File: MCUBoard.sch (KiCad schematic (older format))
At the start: 29 parts

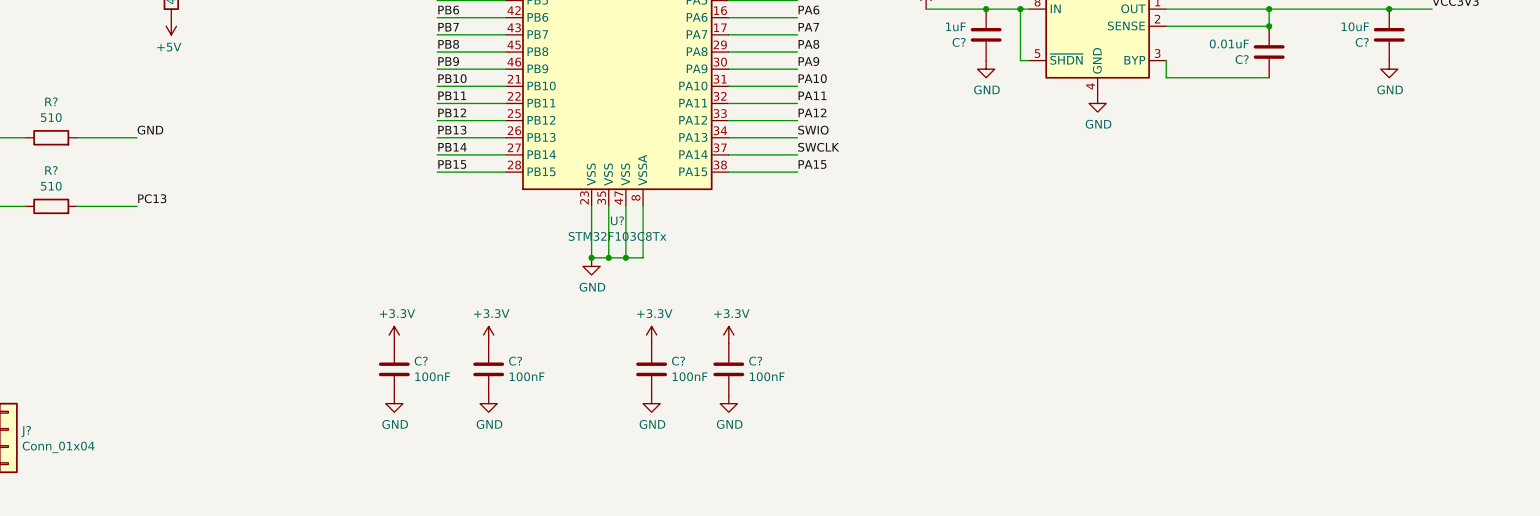
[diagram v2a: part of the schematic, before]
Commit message: added connector for 4D systems uLCD-144-G2
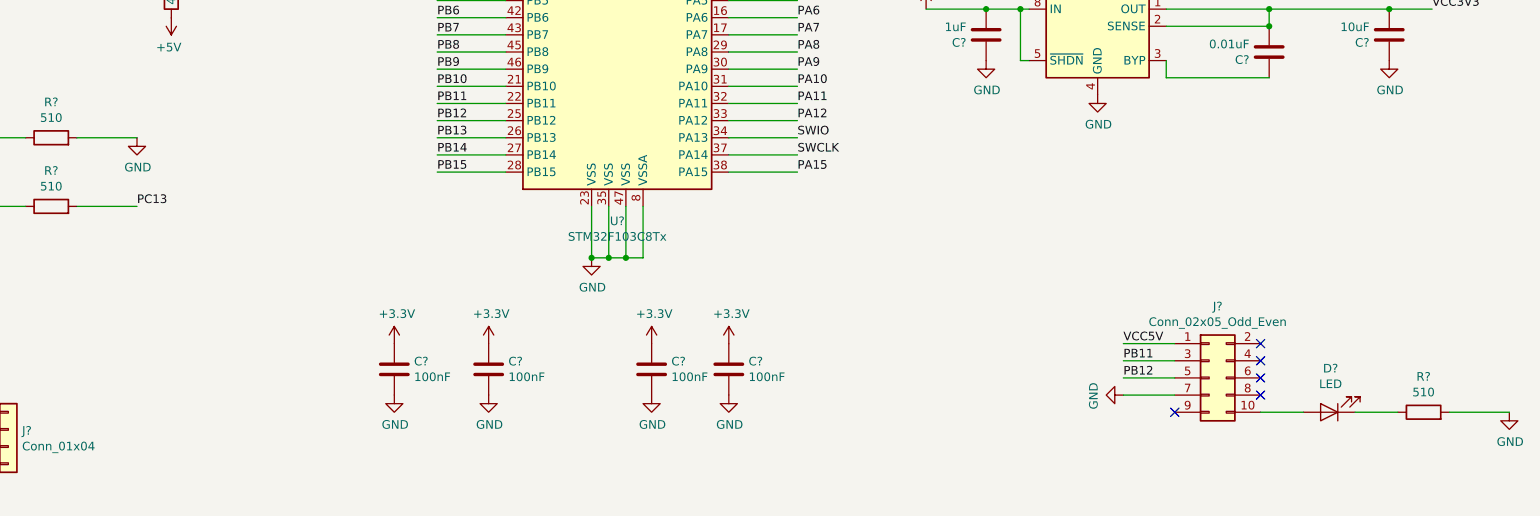
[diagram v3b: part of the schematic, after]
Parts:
- added D?: LED, symbol Device:LED
- added J?: Conn_02x05_Odd_Even, symbol Connector_Generic:Conn_02x05_Odd_Even
- added R?: 510, symbol Device:R
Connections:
- net +5V: now also J?.1 (Pin_1)
- net GND: now also J?.7 (Pin_7), R?.2
- net PB11: now also J?.3 (Pin_3)
- net PB12: now also J?.5 (Pin_5)
- new net: D?.2 (A), J?.10 (Pin_10)
- new net: D?.1 (K), R?.1
- no-connect marks 0 -> 5
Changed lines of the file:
@@
 $EndComp
 $Comp
-L power:GND #PWR?
+L power:GND #PWR0101
 U 1 1 5BB06098
 P 2050 2500
-F 0 "#PWR?" H 2050 2250 50  0001 C CNN
+F 0 "#PWR0101" H 2050 2250 50  0001 C CNN
 F 1 "GND" H 2055 2327 50  0000 C CNN
 F 2 "" H 2050 2500 50  0001 C CNN
@@
 $EndComp
 $Comp
-L power:GND #PWR?
+L power:GND #PWR0102
 U 1 1 5BB060B6
 P 2650 2500
-F 0 "#PWR?" H 2650 2250 50  0001 C CNN
+F 0 "#PWR0102" H 2650 2250 50  0001 C CNN
 F 1 "GND" H 2655 2327 50  0000 C CNN
 F 2 "" H 2650 2500 50  0001 C CNN
@@
 $EndComp
 $Comp
-L power:+3.3V #PWR?
+L power:+3.3V #PWR0103
 U 1 1 5BB06309
 P 2800 2000
-F 0 "#PWR?" H 2800 1850 50  0001 C CNN
+F 0 "#PWR0103" H 2800 1850 50  0001 C CNN
 F 1 "+3.3V" H 2815 2173 50  0000 C CNN
 F 2 "" H 2800 2000 50  0001 C CNN
@@
 BOOT1
 $Comp
-L power:+3.3V #PWR?
+L power:+3.3V #PWR0104
 U 1 1 5BB06604
 P 1900 2000
-F 0 "#PWR?" H 1900 1850 50  0001 C CNN
+F 0 "#PWR0104" H 1900 1850 50  0001 C CNN
 F 1 "+3.3V" H 1915 2173 50  0000 C CNN
 F 2 "" H 1900 2000 50  0001 C CNN
@@
 $EndComp
 $Comp
-L power:+5V #PWR?
+L power:+5V #PWR0105
 U 1 1 5BB0696A
 P 1800 2950
-F 0 "#PWR?" H 1800 2800 50  0001 C CNN
+F 0 "#PWR0105" H 1800 2800 50  0001 C CNN
 F 1 "+5V" H 1815 3123 50  0000 C CNN
 F 2 "" H 1800 2950 50  0001 C CNN
@@
 $EndComp
 $Comp
-L power:GND #PWR?
+L power:GND #PWR0106
 U 1 1 5BB07237
 P 1750 3500
-F 0 "#PWR?" H 1750 3250 50  0001 C CNN
+F 0 "#PWR0106" H 1750 3250 50  0001 C CNN
 F 1 "GND" H 1755 3327 50  0000 C CNN
 F 2 "" H 1750 3500 50  0001 C CNN
@@
 	2850 3500 2850 3400
 $Comp
-L power:+5V #PWR?
+L power:+5V #PWR0107
 U 1 1 5BB07FD5
 P 2850 3800
-F 0 "#PWR?" H 2850 3650 50  0001 C CNN
+F 0 "#PWR0107" H 2850 3650 50  0001 C CNN
 F 1 "+5V" H 2865 3973 50  0000 C CNN
 F 2 "" H 2850 3800 50  0001 C CNN
@@
 $EndComp
 $Comp
-L power:+3.3V #PWR?
+L power:+3.3V #PWR0108
 U 1 1 5BB08511
 P 1200 4400
-F 0 "#PWR?" H 1200 4250 50  0001 C CNN
+F 0 "#PWR0108" H 1200 4250 50  0001 C CNN
 F 1 "+3.3V" H 1215 4573 50  0000 C CNN
 F 2 "" H 1200 4400 50  0001 C CNN
@@
 $EndComp
 $Comp
-L power:+3.3V #PWR?
+L power:+3.3V #PWR0109
 U 1 1 5BB08530
 P 1200 4800
-F 0 "#PWR?" H 1200 4650 50  0001 C CNN
+F 0 "#PWR0109" H 1200 4650 50  0001 C CNN
 F 1 "+3.3V" H 1215 4973 50  0000 C CNN
 F 2 "" H 1200 4800 50  0001 C CNN
@@
 Wire Wire Line
 	2300 4900 2650 4900
-Text Label 2650 4500 0    50   ~ 0
-GND
 Text Label 2650 4900 0    50   ~ 0
 PC13
 $Comp
-L power:+3.3V #PWR?
+L power:+3.3V #PWR0110
 U 1 1 5BB09C56
 P 4150 5700
-F 0 "#PWR?" H 4150 5550 50  0001 C CNN
+F 0 "#PWR0110" H 4150 5550 50  0001 C CNN
 F 1 "+3.3V" H 4165 5873 50  0000 C CNN
 F 2 "" H 4150 5700 50  0001 C CNN
@@
 $EndComp
 $Comp
-L power:GND #PWR?
+L power:GND #PWR0111
 U 1 1 5BB09DA4
 P 4150 6000
-F 0 "#PWR?" H 4150 5750 50  0001 C CNN
+F 0 "#PWR0111" H 4150 5750 50  0001 C CNN
 F 1 "GND" H 4155 5827 50  0000 C CNN
 F 2 "" H 4150 6000 50  0001 C CNN
@@
 $EndComp
 $Comp
-L power:+3.3V #PWR?
+L power:+3.3V #PWR0112
 U 1 1 5BB0A29E
 P 4700 5700
-F 0 "#PWR?" H 4700 5550 50  0001 C CNN
+F 0 "#PWR0112" H 4700 5550 50  0001 C CNN
 F 1 "+3.3V" H 4715 5873 50  0000 C CNN
 F 2 "" H 4700 5700 50  0001 C CNN
@@
 $EndComp
 $Comp
-L power:GND #PWR?
+L power:GND #PWR0113
 U 1 1 5BB0A2AB
 P 4700 6000
-F 0 "#PWR?" H 4700 5750 50  0001 C CNN
+F 0 "#PWR0113" H 4700 5750 50  0001 C CNN
 F 1 "GND" H 4705 5827 50  0000 C CNN
 F 2 "" H 4700 6000 50  0001 C CNN
@@
 $EndComp
 $Comp
-L power:+3.3V #PWR?
+L power:+3.3V #PWR0114
 U 1 1 5BB0A73C
 P 5650 5700
-F 0 "#PWR?" H 5650 5550 50  0001 C CNN
+F 0 "#PWR0114" H 5650 5550 50  0001 C CNN
 F 1 "+3.3V" H 5665 5873 50  0000 C CNN
 F 2 "" H 5650 5700 50  0001 C CNN
@@
 $EndComp
 $Comp
-L power:GND #PWR?
+L power:GND #PWR0115
 U 1 1 5BB0A749
 P 5650 6000
-F 0 "#PWR?" H 5650 5750 50  0001 C CNN
+F 0 "#PWR0115" H 5650 5750 50  0001 C CNN
 F 1 "GND" H 5655 5827 50  0000 C CNN
 F 2 "" H 5650 6000 50  0001 C CNN
@@
 $EndComp
 $Comp
-L power:+3.3V #PWR?
+L power:+3.3V #PWR0116
 U 1 1 5BB0ABDA
 P 6100 5700
-F 0 "#PWR?" H 6100 5550 50  0001 C CNN
+F 0 "#PWR0116" H 6100 5550 50  0001 C CNN
 F 1 "+3.3V" H 6115 5873 50  0000 C CNN
 F 2 "" H 6100 5700 50  0001 C CNN
@@
 $EndComp
 $Comp
-L power:GND #PWR?
+L power:GND #PWR0117
 U 1 1 5BB0ABE7
 P 6100 6000
-F 0 "#PWR?" H 6100 5750 50  0001 C CNN
+F 0 "#PWR0117" H 6100 5750 50  0001 C CNN
 F 1 "GND" H 6105 5827 50  0000 C CNN
 F 2 "" H 6100 6000 50  0001 C CNN
@@
 PC14
 $Comp
-L power:GND #PWR?
+L power:GND #PWR0118
 U 1 1 5BB0CAB3
 P 7500 2400
-F 0 "#PWR?" H 7500 2150 50  0001 C CNN
+F 0 "#PWR0118" H 7500 2150 50  0001 C CNN
 F 1 "GND" H 7505 2227 50  0000 C CNN
 F 2 "" H 7500 2400 50  0001 C CNN
@@
 SWDCLK
 $Comp
-L power:+3.3V #PWR?
+L power:+3.3V #PWR0119
 U 1 1 5BB2C7FE
 P 1150 6100
-F 0 "#PWR?" H 1150 5950 50  0001 C CNN
+F 0 "#PWR0119" H 1150 5950 50  0001 C CNN
 F 1 "+3.3V" H 1165 6273 50  0000 C CNN
 F 2 "" H 1150 6100 50  0001 C CNN
@@
 	1150 6100 1700 6100
 $Comp
-L power:GND #PWR?
+L power:GND #PWR0120
 U 1 1 5BB2C83D
 P 1150 6400
-F 0 "#PWR?" H 1150 6150 50  0001 C CNN
+F 0 "#PWR0120" H 1150 6150 50  0001 C CNN
 F 1 "GND" H 1155 6227 50  0000 C CNN
 F 2 "" H 1150 6400 50  0001 C CNN
@@
 Connection ~ 9250 3750
 $Comp
-L power:GND #PWR?
+L power:GND #PWR0121
 U 1 1 5BB3BDE6
 P 8250 4250
-F 0 "#PWR?" H 8250 4000 50  0001 C CNN
+F 0 "#PWR0121" H 8250 4000 50  0001 C CNN
 F 1 "GND" H 8255 4077 50  0000 C CNN
 F 2 "" H 8250 4250 50  0001 C CNN
@@
 $EndComp
 $Comp
-L power:GND #PWR?
+L power:GND #PWR0122
 U 1 1 5BB3BE2B
 P 7600 4050
-F 0 "#PWR?" H 7600 3800 50  0001 C CNN
+F 0 "#PWR0122" H 7600 3800 50  0001 C CNN
 F 1 "GND" H 7605 3877 50  0000 C CNN
 F 2 "" H 7600 4050 50  0001 C CNN
@@
 $EndComp
 $Comp
-L power:GND #PWR?
+L power:GND #PWR0123
 U 1 1 5BB3BE70
 P 9950 4050
-F 0 "#PWR?" H 9950 3800 50  0001 C CNN
+F 0 "#PWR0123" H 9950 3800 50  0001 C CNN
 F 1 "GND" H 9955 3877 50  0000 C CNN
 F 2 "" H 9950 4050 50  0001 C CNN
@@
 $EndComp
 $Comp
-L power:+5V #PWR?
+L power:+5V #PWR0124
 U 1 1 5BB3C133
 P 7250 3750
-F 0 "#PWR?" H 7250 3600 50  0001 C CNN
+F 0 "#PWR0124" H 7250 3600 50  0001 C CNN
 F 1 "+5V" H 7265 3923 50  0000 C CNN
 F 2 "" H 7250 3750 50  0001 C CNN
@@
 VCC3V3
 $Comp
-L power:GND #PWR?
+L power:GND #PWR0125
 U 1 1 5BB4C12D
 P 5300 5200
-F 0 "#PWR?" H 5300 4950 50  0001 C CNN
+F 0 "#PWR0125" H 5300 4950 50  0001 C CNN
 F 1 "GND" H 5305 5027 50  0000 C CNN
 F 2 "" H 5300 5200 50  0001 C CNN
@@
 Wire Wire Line
 	5500 5200 5600 5200
+$Comp
+L Connector_Generic:Conn_02x05_Odd_Even J?
+U 1 1 5BB50FD8
+P 8900 5900
+F 0 "J?" H 8950 6317 50  0000 C CNN
+F 1 "Conn_02x05_Odd_Even" H 8950 6226 50  0000 C CNN
+F 2 "" H 8900 5900 50  0001 C CNN
+F 3 "~" H 8900 5900 50  0001 C CNN
+	1    8900 5900
+	1    0    0    -1
+$EndComp
+Wire Wire Line
+	8700 5700 8400 5700
+Wire Wire Line
+	8700 5800 8400 5800
+Wire Wire Line
+	8700 5900 8400 5900
+Wire Wire Line
+	8700 6000 8400 6000
+NoConn ~ 9200 5700
+Text Label 8400 5700 0    50   ~ 0
+VCC5V
+Text Label 8400 5800 0    50   ~ 0
+PB11
+Text Label 8400 5900 0    50   ~ 0
+PB12
+$Comp
+L power:GND #PWR?
+U 1 1 5BB91085
+P 8400 6000
+F 0 "#PWR?" H 8400 5750 50  0001 C CNN
+F 1 "GND" H 8405 5827 50  0000 C CNN
+F 2 "" H 8400 6000 50  0001 C CNN
+F 3 "" H 8400 6000 50  0001 C CNN
+	1    8400 6000
+	0    1    1    0
+$EndComp
+NoConn ~ 8700 6100
+NoConn ~ 9200 5800
+NoConn ~ 9200 5900
+NoConn ~ 9200 6000
+$Comp
+L Device:LED D?
+U 1 1 5BBA6862
+P 9600 6100
+F 0 "D?" H 9592 5845 50  0000 C CNN
+F 1 "LED" H 9592 5936 50  0000 C CNN
+F 2 "" H 9600 6100 50  0001 C CNN
+F 3 "~" H 9600 6100 50  0001 C CNN
+	1    9600 6100
+	-1   0    0    1
+$EndComp
+$Comp
+L Device:R R?
+U 1 1 5BBA686F
+P 10150 6100
+F 0 "R?" V 10357 6100 50  0000 C CNN
+F 1 "510" V 10266 6100 50  0000 C CNN
+F 2 "" V 10080 6100 50  0001 C CNN
+F 3 "~" H 10150 6100 50  0001 C CNN
+	1    10150 6100
+	0    -1   -1   0
+$EndComp
+Wire Wire Line
+	9200 6100 9450 6100
+Wire Wire Line
+	9750 6100 10000 6100
+Wire Wire Line
+	10300 6100 10650 6100
+$Comp
+L power:GND #PWR?
+U 1 1 5BBB15E1
+P 2650 4500
+F 0 "#PWR?" H 2650 4250 50  0001 C CNN
+F 1 "GND" H 2655 4327 50  0000 C CNN
+F 2 "" H 2650 4500 50  0001 C CNN
+F 3 "" H 2650 4500 50  0001 C CNN
+	1    2650 4500
+	1    0    0    -1
+$EndComp
+$Comp
+L power:GND #PWR?
+U 1 1 5BBB162C
+P 10650 6100
+F 0 "#PWR?" H 10650 5850 50  0001 C CNN
+F 1 "GND" H 10655 5927 50  0000 C CNN
+F 2 "" H 10650 6100 50  0001 C CNN
+F 3 "" H 10650 6100 50  0001 C CNN
+	1    10650 6100
+	1    0    0    -1
+$EndComp
 $EndSCHEMATC

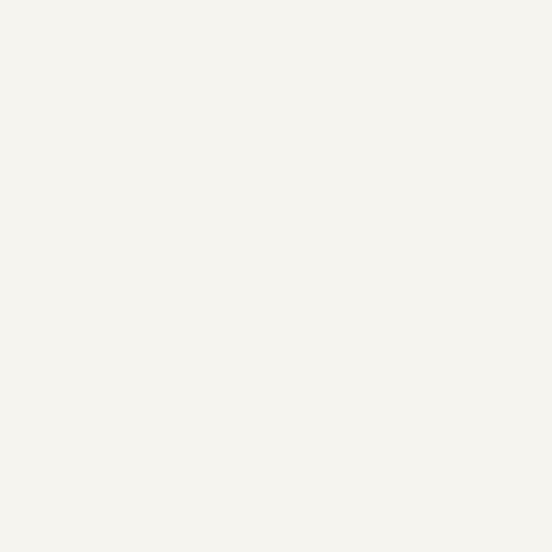
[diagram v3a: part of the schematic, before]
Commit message: 5V-3.3V bidirectional level shifter
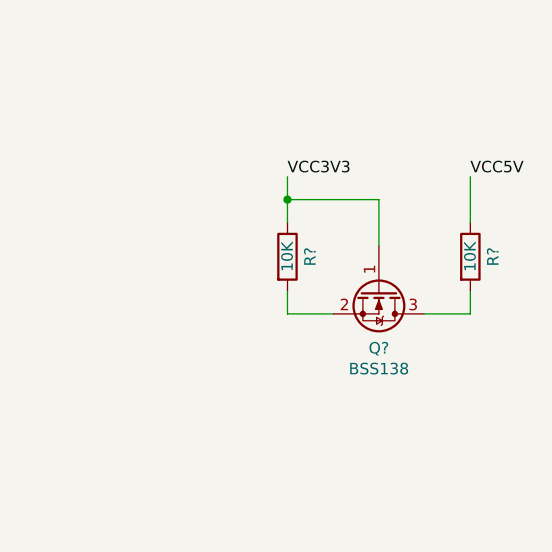
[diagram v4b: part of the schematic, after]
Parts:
- added Q?: BSS138, Package_TO_SOT_SMD:SOT-23, symbol Transistor_FET:BSS138
- added R? (x2): 10K, symbol Device:R
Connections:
- net +5V: now also R?.1
- net VCC3V3: now also Q?.1 (G), R?.1
- new net: Q?.2 (S), R?.2
- new net: Q?.3 (D), R?.2
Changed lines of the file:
@@
 	1    0    0    -1
 $EndComp
+$Comp
+L Device:R R?
+U 1 1 5BBC27EC
+P 11400 2150
+F 0 "R?" V 11500 2150 50  0000 C CNN
+F 1 "10K" V 11400 2150 50  0000 C CNN
+F 2 "" V 11330 2150 50  0001 C CNN
+F 3 "~" H 11400 2150 50  0001 C CNN
+	1    11400 2150
+	1    0    0    -1
+$EndComp
+$Comp
+L Transistor_FET:BSS138 Q?
+U 1 1 5BBC2A16
+P 11800 2300
+F 0 "Q?" V 12050 2300 50  0000 C CNN
+F 1 "BSS138" V 12141 2300 50  0000 C CNN
+F 2 "Package_TO_SOT_SMD:SOT-23" H 12000 2225 50  0001 L CIN
+F 3 "https://www.fairchildsemi.com/datasheets/BS/BSS138.pdf" H 11800 2300 50  0001 L CNN
+	1    11800 2300
+	0    1    1    0
+$EndComp
+$Comp
+L Device:R R?
+U 1 1 5BBCDFE2
+P 12200 2150
+F 0 "R?" V 12300 2150 50  0000 C CNN
+F 1 "10K" V 12200 2150 50  0000 C CNN
+F 2 "" V 12130 2150 50  0001 C CNN
+F 3 "~" H 12200 2150 50  0001 C CNN
+	1    12200 2150
+	1    0    0    -1
+$EndComp
+Wire Wire Line
+	11400 1800 11400 1900
+Wire Wire Line
+	11400 2300 11400 2400
+Wire Wire Line
+	11400 2400 11600 2400
+Wire Wire Line
+	12000 2400 12200 2400
+Wire Wire Line
+	12200 2400 12200 2300
+Wire Wire Line
+	11400 1900 11800 1900
+Wire Wire Line
+	11800 1900 11800 2100
+Connection ~ 11400 1900
+Wire Wire Line
+	11400 1900 11400 2000
+Wire Wire Line
+	12200 2000 12200 1800
+Text Label 11400 1800 0    50   ~ 0
+VCC3V3
+Text Label 12200 1800 0    50   ~ 0
+VCC5V
 $EndSCHEMATC

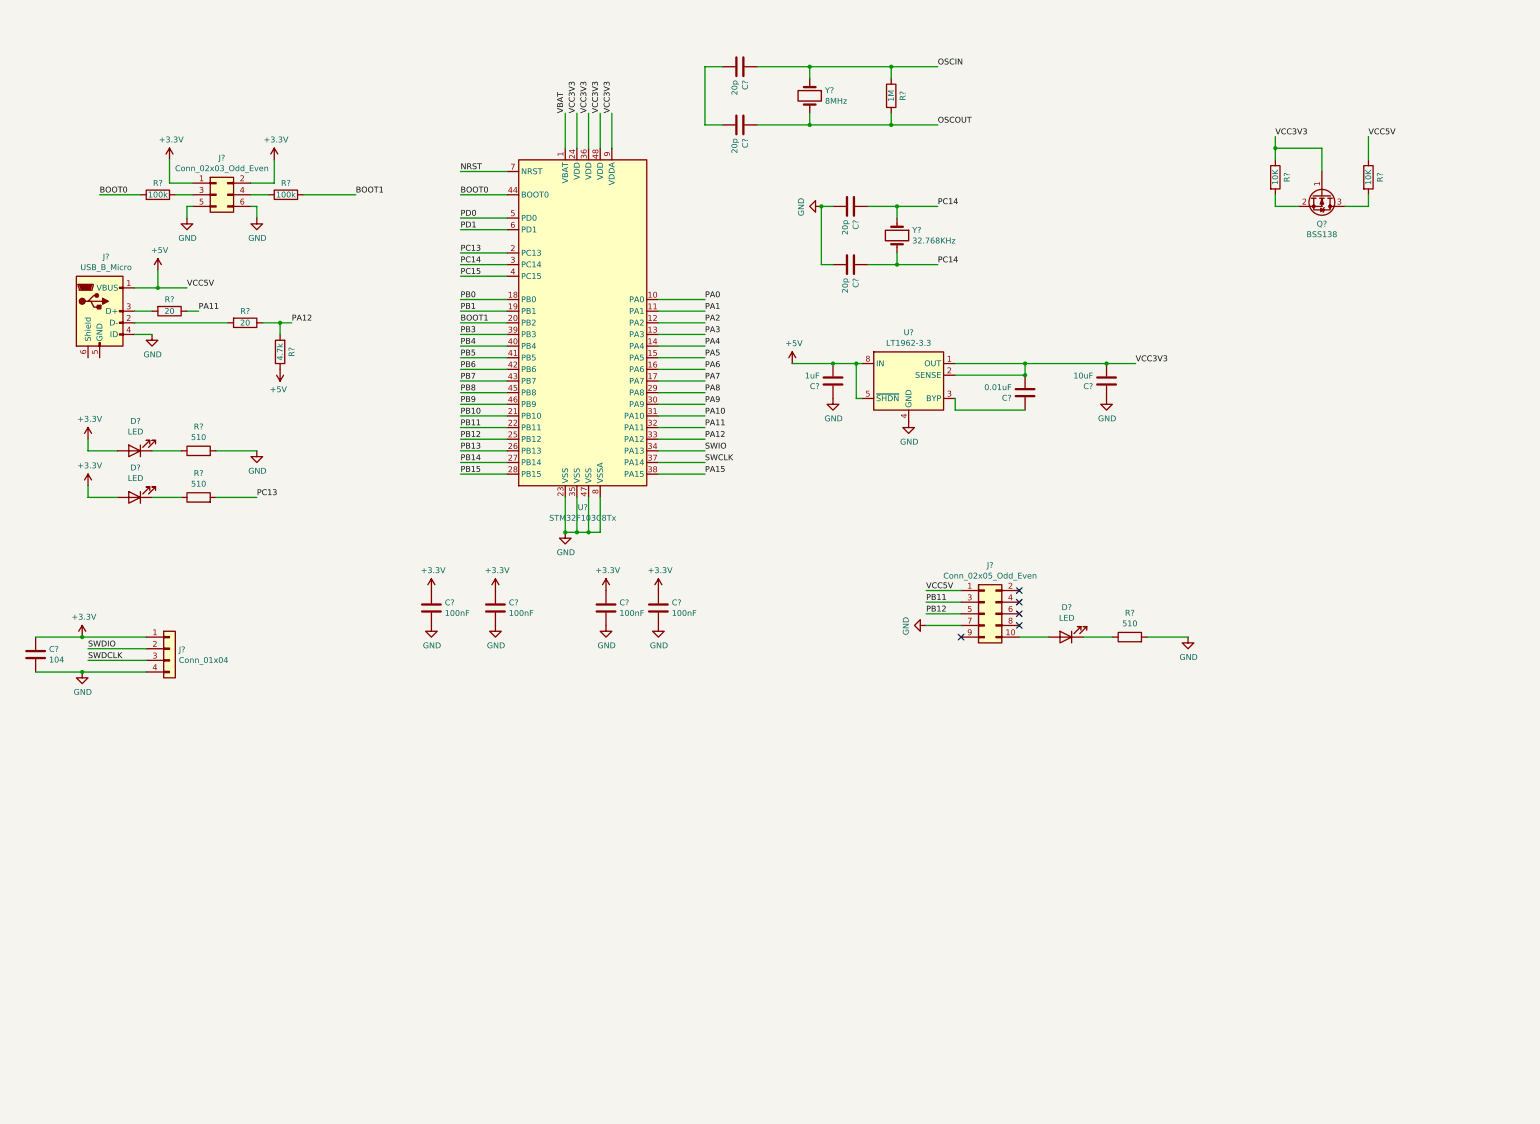
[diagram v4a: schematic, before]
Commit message: add opamps
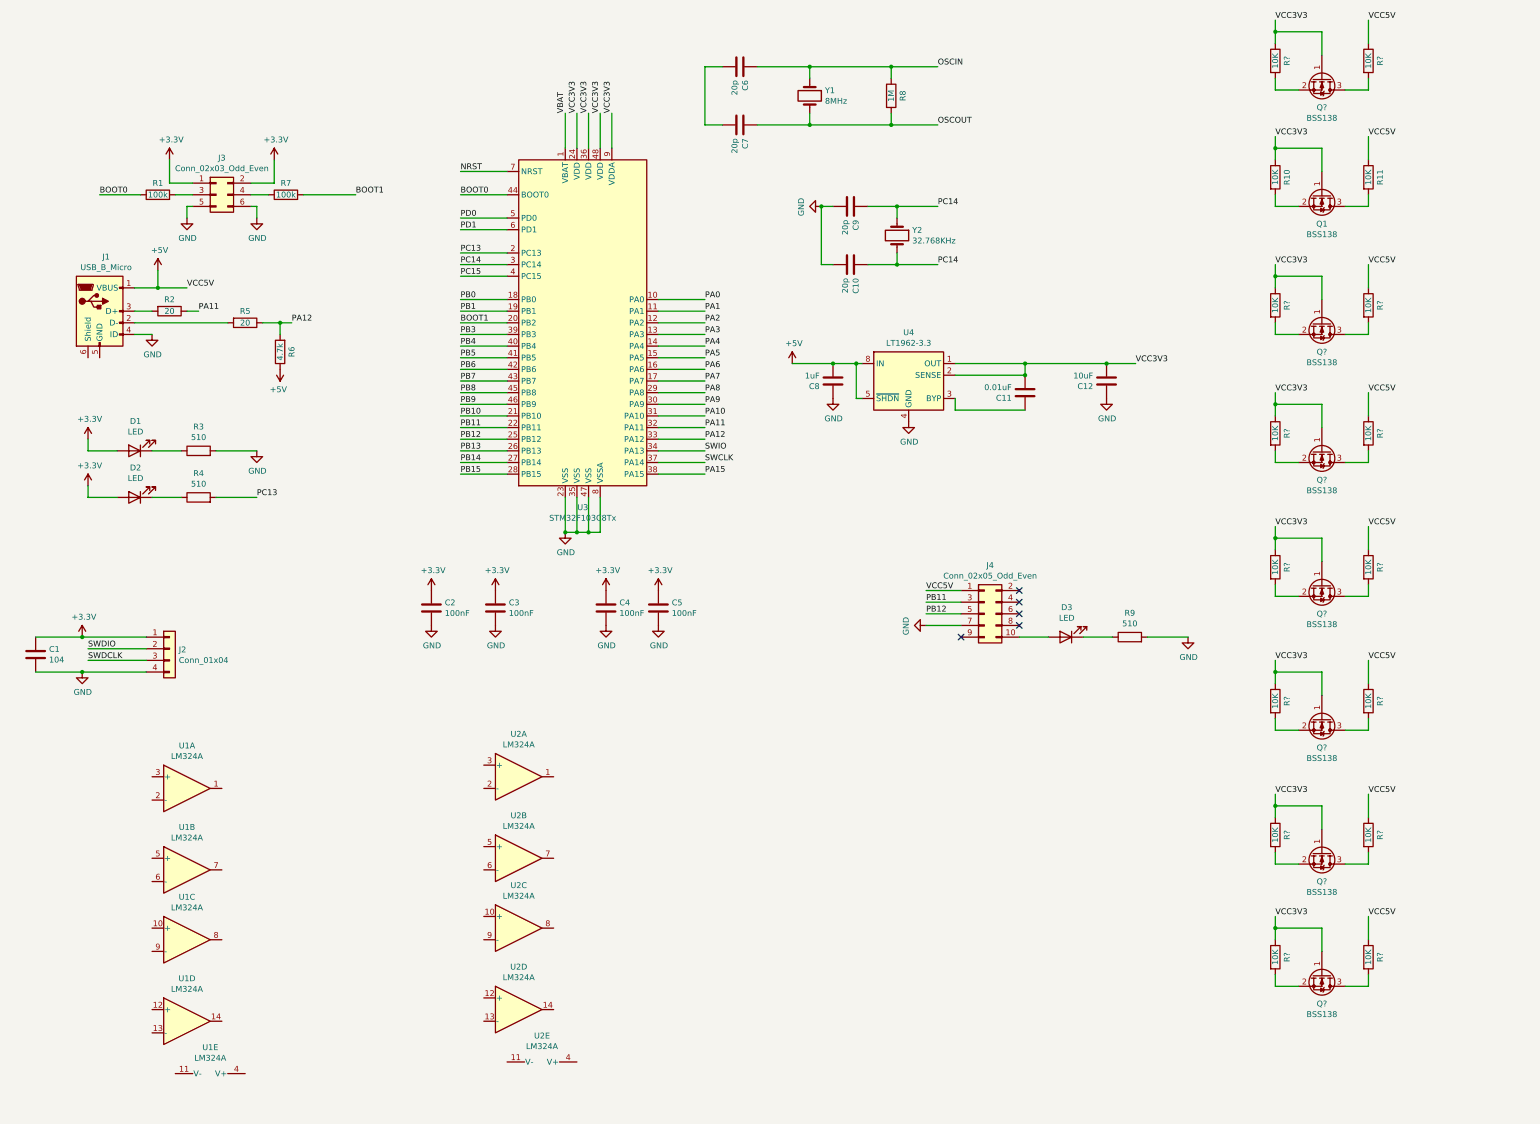
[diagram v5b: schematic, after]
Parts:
- added Q? (x7): BSS138, Package_TO_SOT_SMD:SOT-23, symbol Transistor_FET:BSS138
- added R? (x14): 10K, symbol Device:R
- added U1, U2: LM324A, symbol Amplifier_Operational:LM324A
- gave numbers to parts that had none: 35
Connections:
- net +5V: now also R?.1, R?.1, R?.1, R?.1, R?.1, R?.1, R?.1
- net VCC3V3: now also Q?.1 (G), Q?.1 (G), Q?.1 (G), Q?.1 (G), Q?.1 (G), Q?.1 (G), Q?.1 (G), R?.1, R?.1, R?.1, R?.1, R?.1, R?.1, R?.1
- new net: Q?.2 (S), R?.2 (x7)
- new net: Q?.3 (D), R?.2 (x7)
